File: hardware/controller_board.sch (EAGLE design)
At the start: 46 parts, among them J1 FRSKY-GIMBAL, J2 FRSKY-GIMBAL, J3 WIRE-HARNESS-SPARKFUN-9915, J4 AVR_SPI_PRG_6NS, U1 ATMEGA128RFA1, U2 TPS73633-DBVT, Y1 CRYSTAL5X3

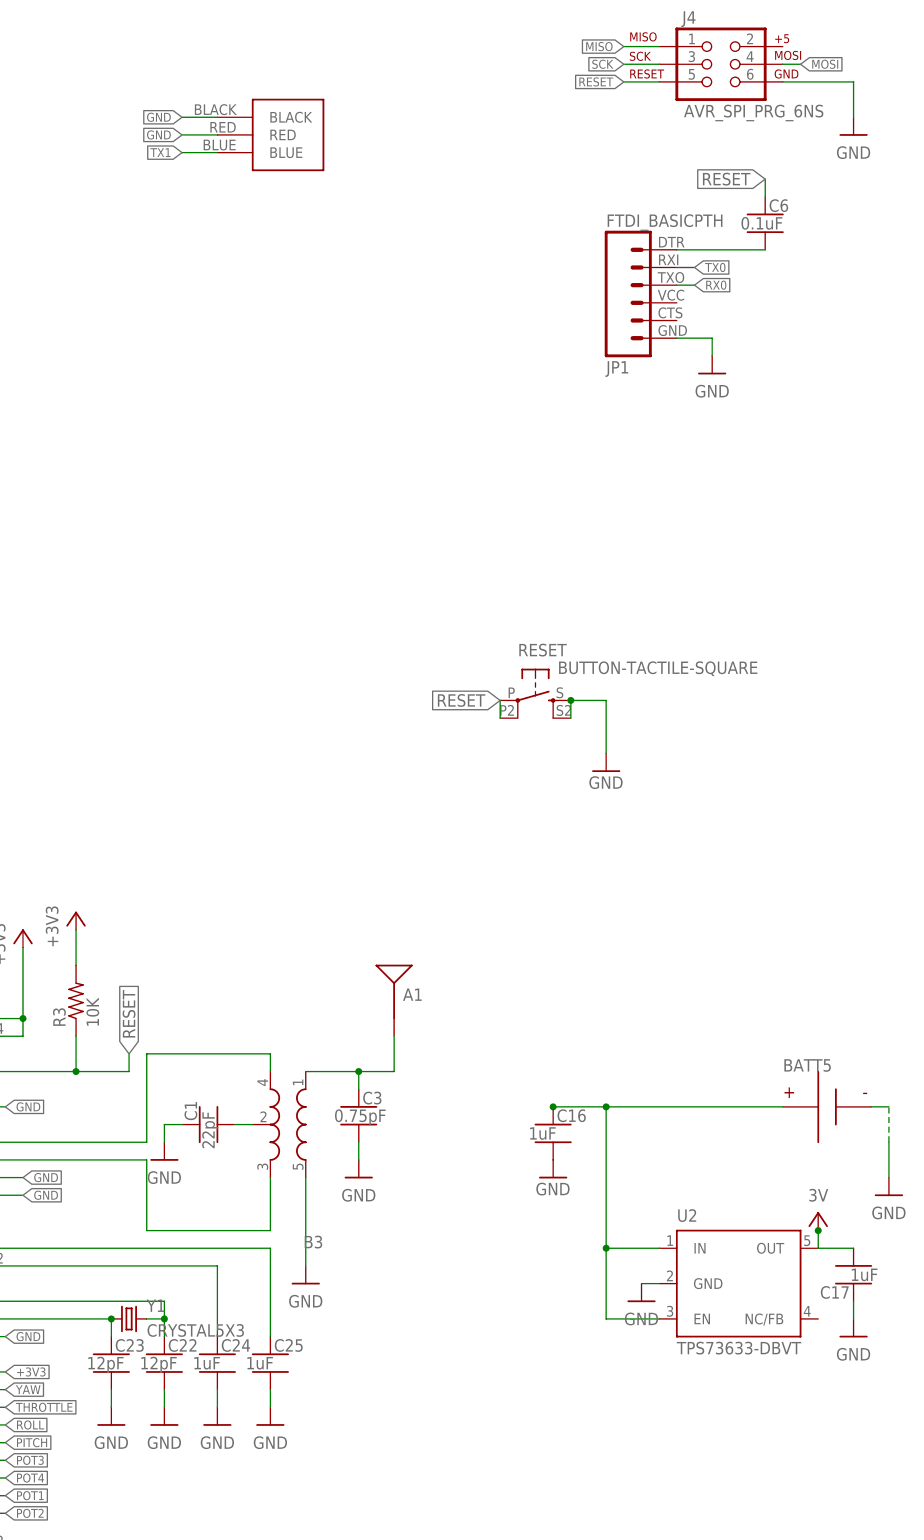
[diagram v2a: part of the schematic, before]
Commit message: fix gnd issue on ISP header
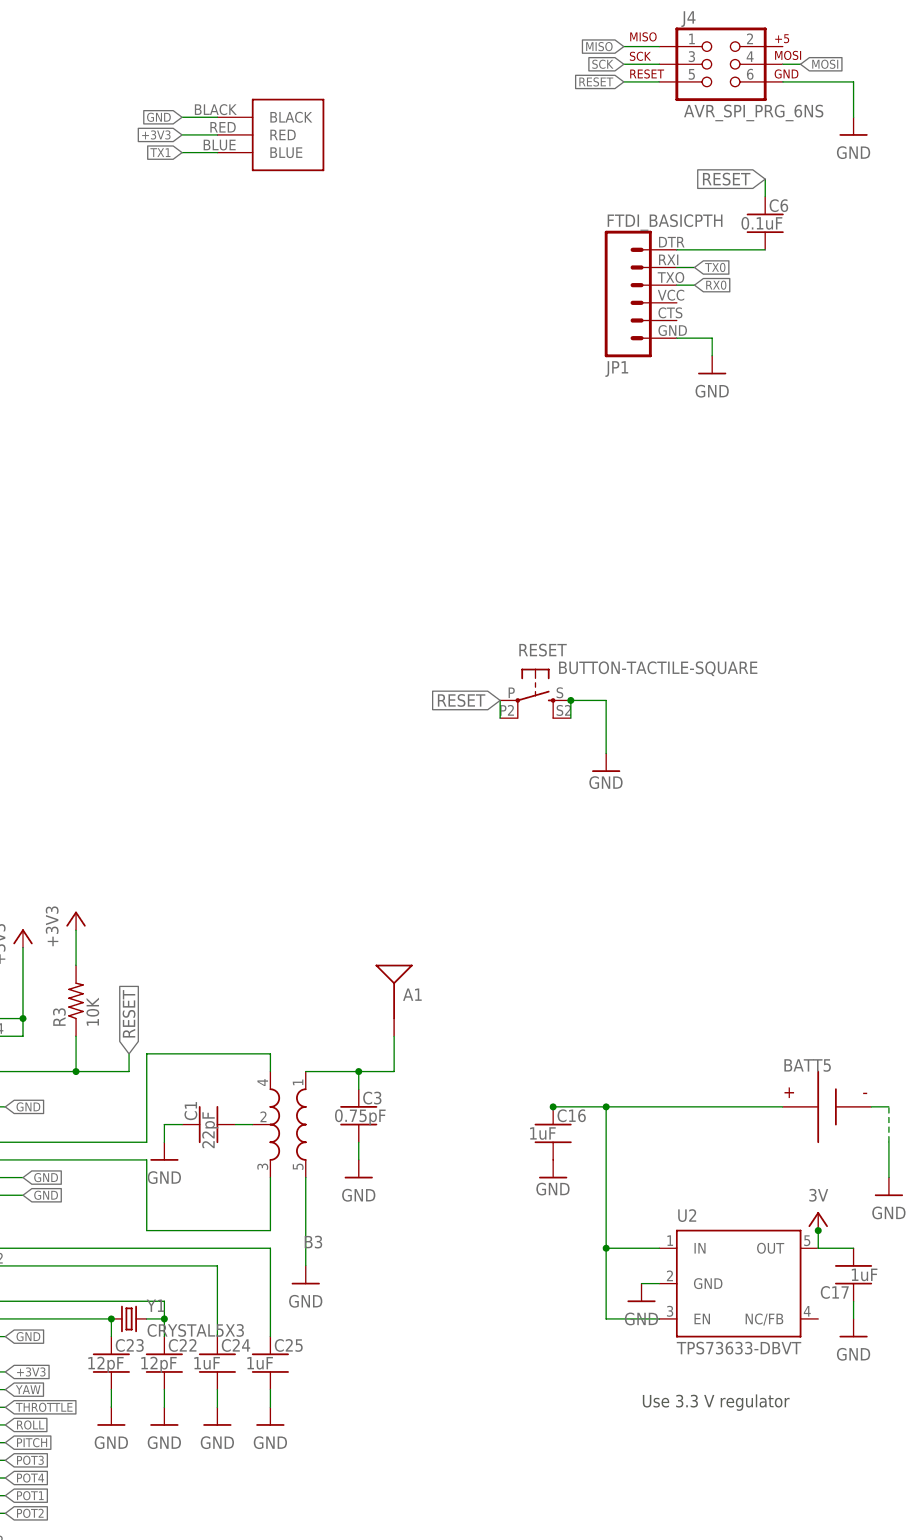
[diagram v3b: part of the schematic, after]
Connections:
- net +3V3: now also J3.RED
- net GND: no longer J3.RED
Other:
- note added: "Use 3.3 V regulator"
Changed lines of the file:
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@@
 <text x="-48.26" y="-27.94" size="1.778" layer="97">Double check other fixes on current boards.</text>
 <text x="-48.26" y="-33.02" size="1.778" layer="97">See notes about aref on board layout.  </text>
+<text x="271.78" y="-33.02" size="1.778" layer="97">Use 3.3 V regulator</text>
 </plain>
 <instances>
@@
 <pinref part="J3" gate="G$1" pin="BLACK"/>
 <wire x1="210.82" y1="152.4" x2="205.74" y2="152.4" width="0.1524" layer="91"/>
-<label x="205.74" y="152.4" size="1.27" layer="91" rot="R180" xref="yes"/>
+<label x="205.74" y="152.4" size="1.27" layer="95" rot="R180" xref="yes"/>
 </segment>
 <segment>
@@
 <wire x1="-38.1" y1="121.92" x2="-43.18" y2="121.92" width="0.1524" layer="91"/>
 <label x="-43.18" y="121.92" size="1.27" layer="95" rot="R180" xref="yes"/>
-</segment>
-<segment>
-<pinref part="J3" gate="G$1" pin="RED"/>
-<wire x1="210.82" y1="149.86" x2="205.74" y2="149.86" width="0.1524" layer="91"/>
-<label x="205.74" y="149.86" size="1.27" layer="91" rot="R180" xref="yes"/>
 </segment>
 <segment>
@@
 <junction x="15.24" y="154.94"/>
 </segment>
-</net>
+<segment>
+<pinref part="J3" gate="G$1" pin="RED"/>
+<wire x1="210.82" y1="149.86" x2="205.74" y2="149.86" width="0.1524" layer="91"/>
+<label x="205.74" y="149.86" size="1.27" layer="95" rot="R180" xref="yes"/>
+</segment>
+</net>

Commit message: cleanup
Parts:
- removed BATT1, BATT2, BATT3, BATT4: BATTERY-AA-CLIP, Components:BATTERY-AA-CLIP
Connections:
- removed net 3V: C17.2, U2.OUT
- removed net N$2: BATT2.N, BATT3.P
- removed net N$3: BATT3.N, BATT4.P
- removed net N$5: BATT1.P, S1.ON
- net +3V3: now also C17.2, U2.OUT
- net GND: no longer BATT4.N, S1.C
- net N$1: now also BATT5.P, S1.ON; no longer BATT1.N, BATT2.P
- net N$6: now also S1.C; no longer BATT5.P
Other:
- note added: "Surface mount: buttons, pwr led, info?, big cap,"
- note added: "What about serial LCD? Check if we can run it off lipo battery. See if we can run it at 3.3 V. If so, we could use a bigger 3.3V regulator. and power everything off of it. Otherwise, use 4xAA and regulate down to 4V. Red board has 2x1uf + 1x10uf decoupling."
- note removed: "What about serial LCD? Check if we can run it off lipo battery. See if we can run it at 3.3 V. If so, we could use a bigger 3.3V regulator. and power everything off of it. Otherwise, use 4xAA and regulate down to 4V."
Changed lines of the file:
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@@
 <parts>
 <part name="B1" library="Controller" deviceset="BUTTON-TACTILE" device="-SQUARE"/>
-<part name="BATT1" library="Components" deviceset="BATTERY" device="-AA-CLIP"/>
-<part name="BATT2" library="Components" deviceset="BATTERY" device="-AA-CLIP"/>
-<part name="BATT3" library="Components" deviceset="BATTERY" device="-AA-CLIP"/>
-<part name="BATT4" library="Components" deviceset="BATTERY" device="-AA-CLIP"/>
 <part name="RESET" library="Controller" deviceset="BUTTON-TACTILE" device="-SQUARE"/>
 <part name="GND4" library="supply1" deviceset="GND" device=""/>
@@
 <part name="GND23" library="quadparts_prebuilt" deviceset="GND" device=""/>
 <part name="GND24" library="quadparts_prebuilt" deviceset="GND" device=""/>
-<part name="P+14" library="quadparts_prebuilt" deviceset="3V" device=""/>
+<part name="P+14" library="supply1" deviceset="+3V3" device=""/>
 <part name="U2" library="quadparts_prebuilt" deviceset="TPS73633-DBVT" device=""/>
 <part name="GND25" library="supply1" deviceset="GND" device=""/>
@@
 <text x="-35.56" y="182.88" size="1.778" layer="97">What about serial LCD?
 Check if we can run it off lipo battery.  See if we can run it at 3.3 V.  If so, we could use a bigger 3.3V regulator. and power everything off of it.
-Otherwise, use 4xAA and regulate down to 4V.</text>
+Otherwise, use 4xAA and regulate down to 4V.
+Red board has 2x1uf + 1x10uf decoupling.</text>
 <text x="-48.26" y="-22.86" size="1.778" layer="97">Double check button polarity.</text>
 <text x="-48.26" y="-27.94" size="1.778" layer="97">Double check other fixes on current boards.</text>
 <text x="-48.26" y="-33.02" size="1.778" layer="97">See notes about aref on board layout.  </text>
 <text x="271.78" y="-33.02" size="1.778" layer="97">Use 3.3 V regulator</text>
+<text x="-35.56" y="177.8" size="1.778" layer="97" align="top-left">Surface mount:
+buttons,
+pwr led,
+info?,
+big cap,
+</text>
 </plain>
 <instances>
 <instance part="B1" gate="G$1" x="78.74" y="134.62" rot="R270"/>
-<instance part="BATT1" gate="G$1" x="-10.16" y="124.46"/>
-<instance part="BATT2" gate="G$1" x="5.08" y="124.46"/>
-<instance part="BATT3" gate="G$1" x="20.32" y="124.46"/>
-<instance part="BATT4" gate="G$1" x="35.56" y="124.46"/>
 <instance part="RESET" gate="G$1" x="256.54" y="68.58" rot="R270"/>
 <instance part="GND4" gate="1" x="266.7" y="58.42"/>
@@
 <instance part="+3V3" gate="G$1" x="162.56" y="144.78"/>
 <instance part="GND5" gate="1" x="162.56" y="129.54"/>
-<instance part="S1" gate="G$1" x="-22.86" y="119.38"/>
+<instance part="S1" gate="G$1" x="281.94" y="7.62"/>
 <instance part="LED1" gate="G$1" x="30.48" y="154.94"/>
 <instance part="+3V4" gate="G$1" x="30.48" y="162.56"/>
@@
 </segment>
 <segment>
-<pinref part="BATT4" gate="G$1" pin="N"/>
-<wire x1="43.18" y1="124.46" x2="40.64" y2="124.46" width="0.1524" layer="91"/>
-<label x="43.18" y="124.46" size="1.27" layer="95" xref="yes"/>
-</segment>
-<segment>
 <pinref part="GND" gate="G$1" pin="3"/>
 <pinref part="GND" gate="G$1" pin="1"/>
@@
 </segment>
 <segment>
-<pinref part="S1" gate="G$1" pin="C"/>
-<wire x1="-38.1" y1="121.92" x2="-43.18" y2="121.92" width="0.1524" layer="91"/>
-<label x="-43.18" y="121.92" size="1.27" layer="95" rot="R180" xref="yes"/>
-</segment>
-<segment>
 <pinref part="C16" gate="G$1" pin="2"/>
 <pinref part="GND25" gate="1" pin="GND"/>
@@
 <label x="205.74" y="149.86" size="1.27" layer="95" rot="R180" xref="yes"/>
 </segment>
+<segment>
+<pinref part="C17" gate="G$1" pin="2"/>
+<pinref part="P+14" gate="G$1" pin="+3V3"/>
+<pinref part="U2" gate="G$1" pin="OUT"/>
+<wire x1="297.18" y1="-10.16" x2="302.26" y2="-10.16" width="0.1524" layer="91"/>
+<junction x="297.18" y="-7.62"/>
+<wire x1="297.18" y1="-7.62" x2="297.18" y2="-10.16" width="0.1524" layer="91"/>
+</segment>
 </net>
 <net name="TX1" class="0">
@@
 <wire x1="121.92" y1="-7.62" x2="119.38" y2="-7.62" width="0.1524" layer="91" style="longdash"/>
 <label x="119.38" y="-7.62" size="1.27" layer="95" font="fixed" rot="R180" xref="yes"/>
-</segment>
-</net>
-<net name="N$1" class="1">
-<segment>
-<pinref part="BATT1" gate="G$1" pin="N"/>
-<pinref part="BATT2" gate="G$1" pin="P"/>
-<wire x1="-5.08" y1="124.46" x2="-2.54" y2="124.46" width="0.1524" layer="91"/>
-</segment>
-</net>
-<net name="N$2" class="1">
-<segment>
-<pinref part="BATT2" gate="G$1" pin="N"/>
-<pinref part="BATT3" gate="G$1" pin="P"/>
-<wire x1="12.7" y1="124.46" x2="10.16" y2="124.46" width="0.1524" layer="91"/>
-</segment>
-</net>
-<net name="N$3" class="1">
-<segment>
-<pinref part="BATT3" gate="G$1" pin="N"/>
-<pinref part="BATT4" gate="G$1" pin="P"/>
-<wire x1="27.94" y1="124.46" x2="25.4" y2="124.46" width="0.1524" layer="91"/>
 </segment>
 </net>
@@
 </segment>
 </net>
-<net name="N$5" class="1">
-<segment>
-<pinref part="BATT1" gate="G$1" pin="P"/>
-<pinref part="S1" gate="G$1" pin="ON"/>
-<wire x1="-20.32" y1="124.46" x2="-17.78" y2="124.46" width="0.1524" layer="91"/>
-</segment>
-</net>
 <net name="POT2" class="0">
 <segment>
@@
 <pinref part="JP1" gate="G$1" pin="1"/>
 <wire x1="276.86" y1="133.35" x2="289.56" y2="133.35" width="0.1524" layer="91"/>
-</segment>
-</net>
-<net name="3V" class="0">
-<segment>
-<pinref part="C17" gate="G$1" pin="2"/>
-<pinref part="P+14" gate="G$1" pin="3V"/>
-<pinref part="U2" gate="G$1" pin="OUT"/>
-<wire x1="297.18" y1="-10.16" x2="302.26" y2="-10.16" width="0.1524" layer="91"/>
-<junction x="297.18" y="-7.62"/>
-<wire x1="297.18" y1="-7.62" x2="297.18" y2="-10.16" width="0.1524" layer="91"/>
 </segment>
 </net>
@@
 <junction x="266.7" y="-10.16"/>
 <junction x="266.7" y="10.16"/>
+<pinref part="S1" gate="G$1" pin="C"/>
+</segment>
+</net>
+<net name="N$1" class="0">
+<segment>
 <pinref part="BATT5" gate="G$1" pin="P"/>
-<wire x1="266.7" y1="10.16" x2="292.1" y2="10.16" width="0.1524" layer="91"/>
-</segment>
-</net>
+<pinref part="S1" gate="G$1" pin="ON"/>
+<wire x1="284.48" y1="12.7" x2="292.1" y2="12.7" width="0.1524" layer="91"/>
+<wire x1="292.1" y1="12.7" x2="292.1" y2="10.16" width="0.1524" layer="91"/>
+</segment>
+</net>

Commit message: small fixes. going through check list
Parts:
- added C7: (no value), KoalaBuild:RESOLVED-CAPACITOR-POL_TH-RADIAL_ALUMINUM_6.3MM
- added J5: (no value), Components:HEADER-0.1IN-3POS-MALE
- added J6: (no value), custom:MALE_HEADER_2POS-2X1-0.1IN
- added R4, R5: 10K, quadparts_prebuilt:RESISTOR_SMD-2012-0805-10K
- BATT5: value BATTERY-HUBSAN-W/HOLDER -> BATTERY; device quadparts_prebuilt:BATTERY-HUBSAN-W/HOLDER -> quadparts_prebuilt:BATTERY
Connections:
- removed net N$6: C16.1, S1.C, U2.EN, U2.IN
- new net AREF: J6.1, U1.AREF
- new net GREF: J1.VCC-H, J1.VCC-V, J2.VCC-H, J2.VCC-V, J5.2, TM1.E, TM2.E, TM3.E, TM4.E
- new net N$5: J5.3, R4.1, R5.2
- net +3V3: now also J5.1, J6.2, R4.2; no longer J1.VCC-H, J1.VCC-V, J2.VCC-H, J2.VCC-V, J3.RED, TM1.E, TM2.E, TM3.E, TM4.E, U1.AREF
- net GND: now also C7.-, R5.1
- net VBAT: now also C16.1, C7.+, S1.C, U2.EN, U2.IN, VBAT.1
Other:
- note added: "Connect power to +3v3 or VBAT?"
- note added: "Double check button polarity. Seem right confirm with fixed boards."
- note added: "For next rev: Red board has 2x1uf + 2x10uf decoupling. instead of 2x100uf"
- note added: "Use 3.3 V regulator LP3985IM5‑3.3/NOPBCT‑ND https://www.digikey.com/product-detail/en/texas-instruments/LP3985IM5-3.3-NOPB/LP3985IM5-3.3-NOPBCT-ND/562199"
- note added: "What about serial LCD? Check if we can run it off lipo battery. See if we can run it at 3.3 V. If so, we could use a bigger 3.3V regulator. and power everything off of it. Otherwise, use 4xAA and regulate down to 4V."
- note removed: "Double check button polarity."
- note removed: "Use 3.3 V regulator"
- note removed: "What about serial LCD? Check if we can run it off lipo battery. See if we can run it at 3.3 V. If so, we could use a bigger 3.3V regulator. and power everything off of it. Otherwise, use 4xAA and regulate down to 4V. Red board has 2x1uf + 1x10uf decoupling."
- moved on the sheet: 3.3V, C2, GND, JP1, LED1, RESET, TM1, TM2, VBAT

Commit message: Rev1-rc1
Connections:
- net VBAT: now also J3.RED
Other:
- note removed: "Connect power to +3v3 or VBAT?"
- note removed: "Double check button polarity. Seem right confirm with fixed boards."
- note removed: "Double check other fixes on current boards."
- note removed: "See notes about aref on board layout."
- note removed: "What about serial LCD? Check if we can run it off lipo battery. See if we can run it at 3.3 V. If so, we could use a bigger 3.3V regulator. and power everything off of it. Otherwise, use 4xAA and regulate down to 4V."
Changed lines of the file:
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@@
 <text x="314.96" y="-27.94" size="1.778" layer="97">Power LED</text>
 <text x="127" y="114.3" size="1.778" layer="97">Potentiameter</text>
-<text x="-35.56" y="182.88" size="1.778" layer="97">What about serial LCD?
-Check if we can run it off lipo battery.  See if we can run it at 3.3 V.  If so, we could use a bigger 3.3V regulator. and power everything off of it.
-Otherwise, use 4xAA and regulate down to 4V.
-</text>
-<text x="-48.26" y="-22.86" size="1.778" layer="97">Double check button polarity.  Seem right confirm with fixed boards.</text>
-<text x="-48.26" y="-27.94" size="1.778" layer="97">Double check other fixes on current boards.</text>
-<text x="-48.26" y="-33.02" size="1.778" layer="97">See notes about aref on board layout.  </text>
 <text x="271.78" y="-40.64" size="1.778" layer="97">Use 3.3 V regulator
 LP3985IM5‑3.3/NOPBCT‑ND
@@
 big cap,
 </text>
-<text x="200.66" y="160.02" size="1.778" layer="97">Connect power to +3v3 or VBAT?</text>
 <text x="271.78" y="-48.26" size="1.27" layer="97">For next rev:  Red board has 2x1uf + 2x10uf decoupling.  instead of 2x100uf</text>
-<rectangle x1="193.04" y1="124.46" x2="243.84" y2="172.72" layer="91"/>
 </plain>
 <instances>
@@
 <wire x1="259.08" y1="10.16" x2="251.46" y2="10.16" width="0.1524" layer="91"/>
 </segment>
-</net>
+<segment>
+<pinref part="J3" gate="G$1" pin="RED"/>
+<wire x1="210.82" y1="149.86" x2="205.74" y2="149.86" width="0.1524" layer="91"/>
+<label x="205.74" y="149.86" size="1.27" layer="95" rot="R180" xref="yes"/>
+</segment>
+</net>

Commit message: taped out for jlcpcb
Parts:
- renumbered JP1 to J7, LED1 to D4, LED_Y to D1
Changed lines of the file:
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@@
 <part name="GND5" library="supply1" deviceset="GND" device=""/>
 <part name="S1" library="RemoteParts" deviceset="POWER-SWITCH-MFS201N-9-Z" device=""/>
-<part name="LED1" library="Components" deviceset="LED" device="-5MM-RED">
+<part name="D4" library="Components" deviceset="LED" device="-5MM-RED">
 <attribute name="DISTPN" value="679"/>
 </part>
@@
 <part name="GND18" library="quadparts_prebuilt" deviceset="GND" device=""/>
 <part name="GND19" library="quadparts_prebuilt" deviceset="GND" device=""/>
-<part name="LED_Y" library="custom" deviceset="LED" device="CMD17" value="2V - 20mA"/>
+<part name="D1" library="custom" deviceset="LED" device="CMD17" value="2V - 20mA"/>
 <part name="P+10" library="supply1" deviceset="+3V3" device=""/>
 <part name="P+1" library="supply1" deviceset="+3V3" device=""/>
@@
 <part name="C6" library="quadparts_prebuilt" deviceset="CAPACITOR-NP_" device="SMD-2012-0805_CERAMIC-0.1UF" value="0.1uF"/>
 <part name="GND21" library="quadparts_prebuilt" deviceset="GND" device=""/>
-<part name="JP1" library="quadparts_prebuilt" deviceset="FTDI_BASIC" device="PTH"/>
+<part name="J7" library="quadparts_prebuilt" deviceset="FTDI_BASIC" device="PTH"/>
 <part name="BATT5" library="quadparts_prebuilt" deviceset="BATTERY" device="" value="BATTERY"/>
 <part name="C16" library="quadparts_prebuilt" deviceset="CAPACITOR-NP_" device="SMD-2012-0805_CERAMIC-1UF" value="1uF"/>
@@
 <instance part="GND5" gate="1" x="162.56" y="121.92"/>
 <instance part="S1" gate="G$1" x="281.94" y="7.62"/>
-<instance part="LED1" gate="G$1" x="317.5" y="-12.7"/>
+<instance part="D4" gate="G$1" x="317.5" y="-12.7"/>
 <instance part="GND7" gate="1" x="317.5" y="-20.32"/>
 <instance part="J3" gate="G$1" x="220.98" y="149.86" rot="R180"/>
@@
 <instance part="GND18" gate="1" x="73.66" y="7.62"/>
 <instance part="GND19" gate="1" x="73.66" y="0"/>
-<instance part="LED_Y" gate="G$1" x="88.9" y="-35.56" rot="R180"/>
+<instance part="D1" gate="G$1" x="88.9" y="-35.56" rot="R180"/>
 <instance part="P+10" gate="G$1" x="190.5" y="38.1"/>
 <instance part="P+1" gate="G$1" x="182.88" y="35.56"/>
@@
 <instance part="C6" gate="G$1" x="289.56" y="138.43"/>
 <instance part="GND21" gate="1" x="281.94" y="115.57"/>
-<instance part="JP1" gate="G$1" x="269.24" y="128.27" rot="MR180"/>
+<instance part="J7" gate="G$1" x="269.24" y="128.27" rot="MR180"/>
 <instance part="BATT5" gate="G$1" x="299.72" y="10.16"/>
 <instance part="C16" gate="G$1" x="259.08" y="7.62"/>
@@
 <segment>
 <pinref part="GND7" gate="1" pin="GND"/>
-<pinref part="LED1" gate="G$1" pin="C"/>
+<pinref part="D4" gate="G$1" pin="C"/>
 </segment>
 <segment>
@@
 <segment>
 <pinref part="GND29" gate="1" pin="GND"/>
-<pinref part="LED_Y" gate="G$1" pin="C"/>
+<pinref part="D1" gate="G$1" pin="C"/>
 <wire x1="83.82" y1="-35.56" x2="76.2" y2="-35.56" width="0.1524" layer="91"/>
 </segment>
@@
 <segment>
 <pinref part="GND21" gate="1" pin="GND"/>
-<pinref part="JP1" gate="G$1" pin="6"/>
+<pinref part="J7" gate="G$1" pin="6"/>
 <wire x1="274.32" y1="120.65" x2="281.94" y2="120.65" width="0.1524" layer="91"/>
 <wire x1="281.94" y1="120.65" x2="281.94" y2="118.11" width="0.1524" layer="91"/>
@@
 <pinref part="C2" gate="G$1" pin="+"/>
 <wire x1="309.88" y1="-10.16" x2="302.26" y2="-10.16" width="0.1524" layer="91"/>
-<pinref part="LED1" gate="G$1" pin="A"/>
+<pinref part="D4" gate="G$1" pin="A"/>
 <wire x1="309.88" y1="-10.16" x2="317.5" y2="-10.16" width="0.1524" layer="91"/>
 <junction x="309.88" y="-10.16"/>
@@
 <net name="N$18" class="0">
 <segment>
-<pinref part="LED_Y" gate="G$1" pin="A"/>
+<pinref part="D1" gate="G$1" pin="A"/>
 <pinref part="R17" gate="G$1" pin="1"/>
 <wire x1="96.52" y1="-35.56" x2="93.98" y2="-35.56" width="0.1524" layer="91"/>
@@
 </segment>
 <segment>
-<pinref part="JP1" gate="G$1" pin="3"/>
+<pinref part="J7" gate="G$1" pin="3"/>
 <wire x1="274.32" y1="128.27" x2="279.4" y2="128.27" width="0.1524" layer="91"/>
 <label x="279.4" y="128.27" size="1.27" layer="95" font="fixed" xref="yes"/>
@@
 </segment>
 <segment>
-<pinref part="JP1" gate="G$1" pin="2"/>
+<pinref part="J7" gate="G$1" pin="2"/>
 <wire x1="279.4" y1="130.81" x2="274.32" y2="130.81" width="0.1524" layer="91"/>
 <label x="279.4" y="130.81" size="1.27" layer="95" font="fixed" xref="yes"/>
@@
 <segment>
 <pinref part="C6" gate="G$1" pin="2"/>
-<pinref part="JP1" gate="G$1" pin="1"/>
+<pinref part="J7" gate="G$1" pin="1"/>
 <wire x1="274.32" y1="133.35" x2="289.56" y2="133.35" width="0.1524" layer="91"/>
 </segment>
